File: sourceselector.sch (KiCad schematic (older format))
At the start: 31 parts, among them J14 RCAJack, J15 RCAJack, J16 RCAJack, J17 RCAJack, J18 RCAJack, J19 RCAJack, J20 RCAJack, J21 RCAJack, J22 Jack-DC, J23 Conn_01x02, J24 Conn_01x02, SW2 SW_SPST, SW3 SW_SPST

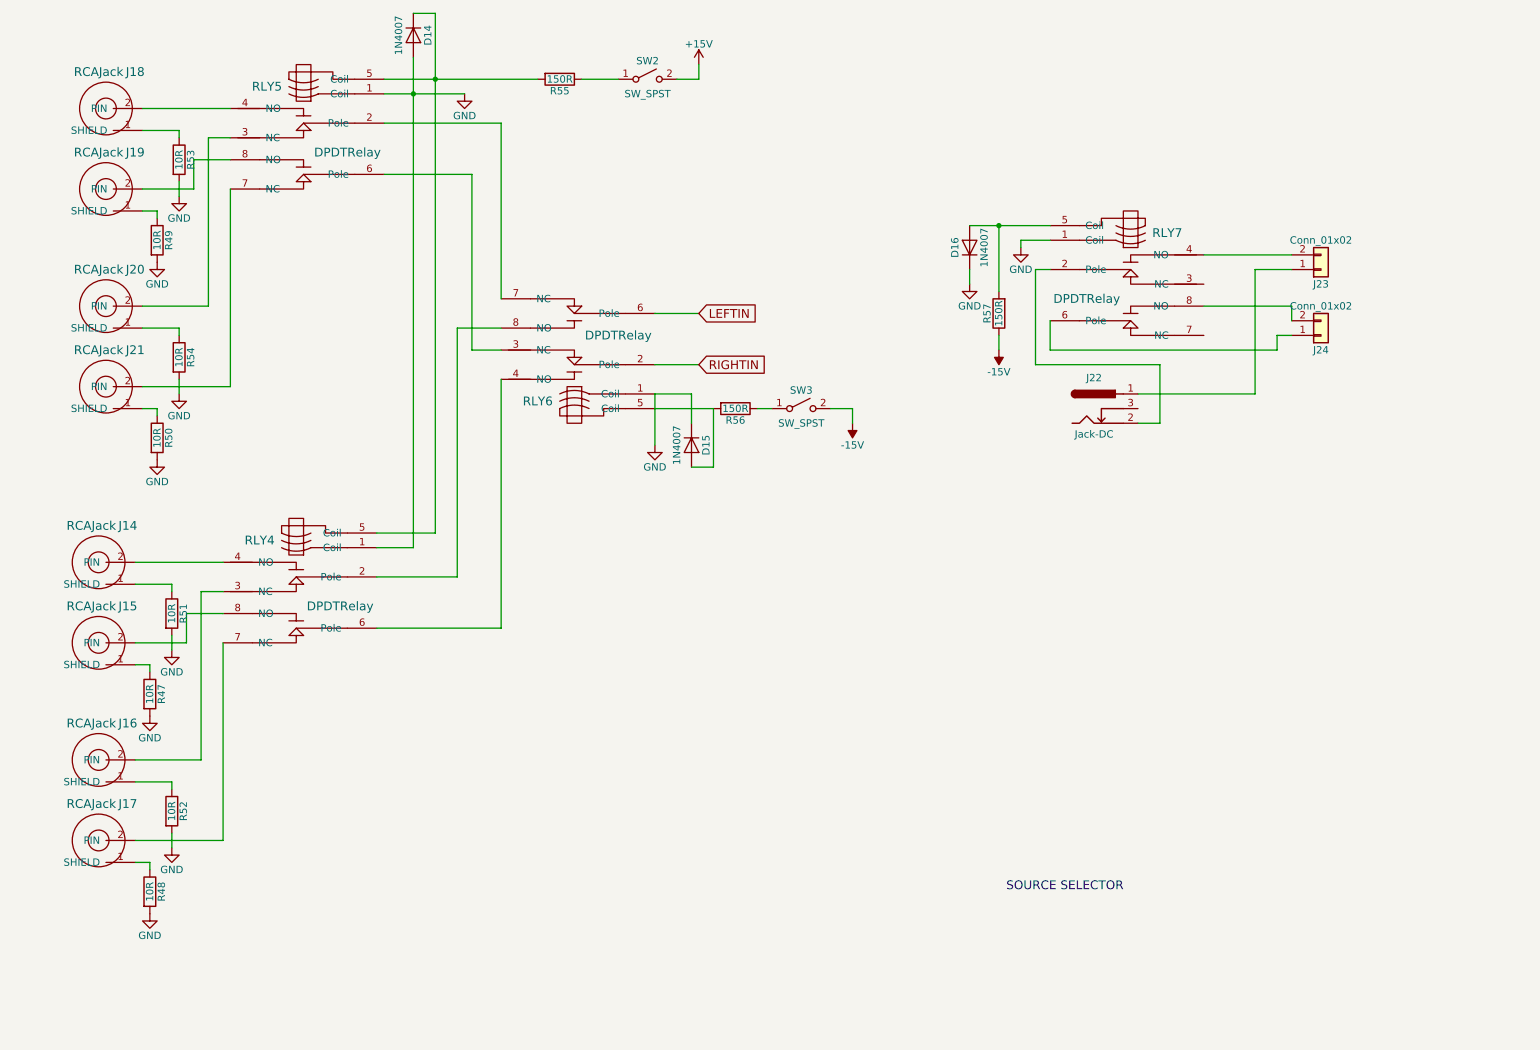
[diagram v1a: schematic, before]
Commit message: Changed one input to be balanced
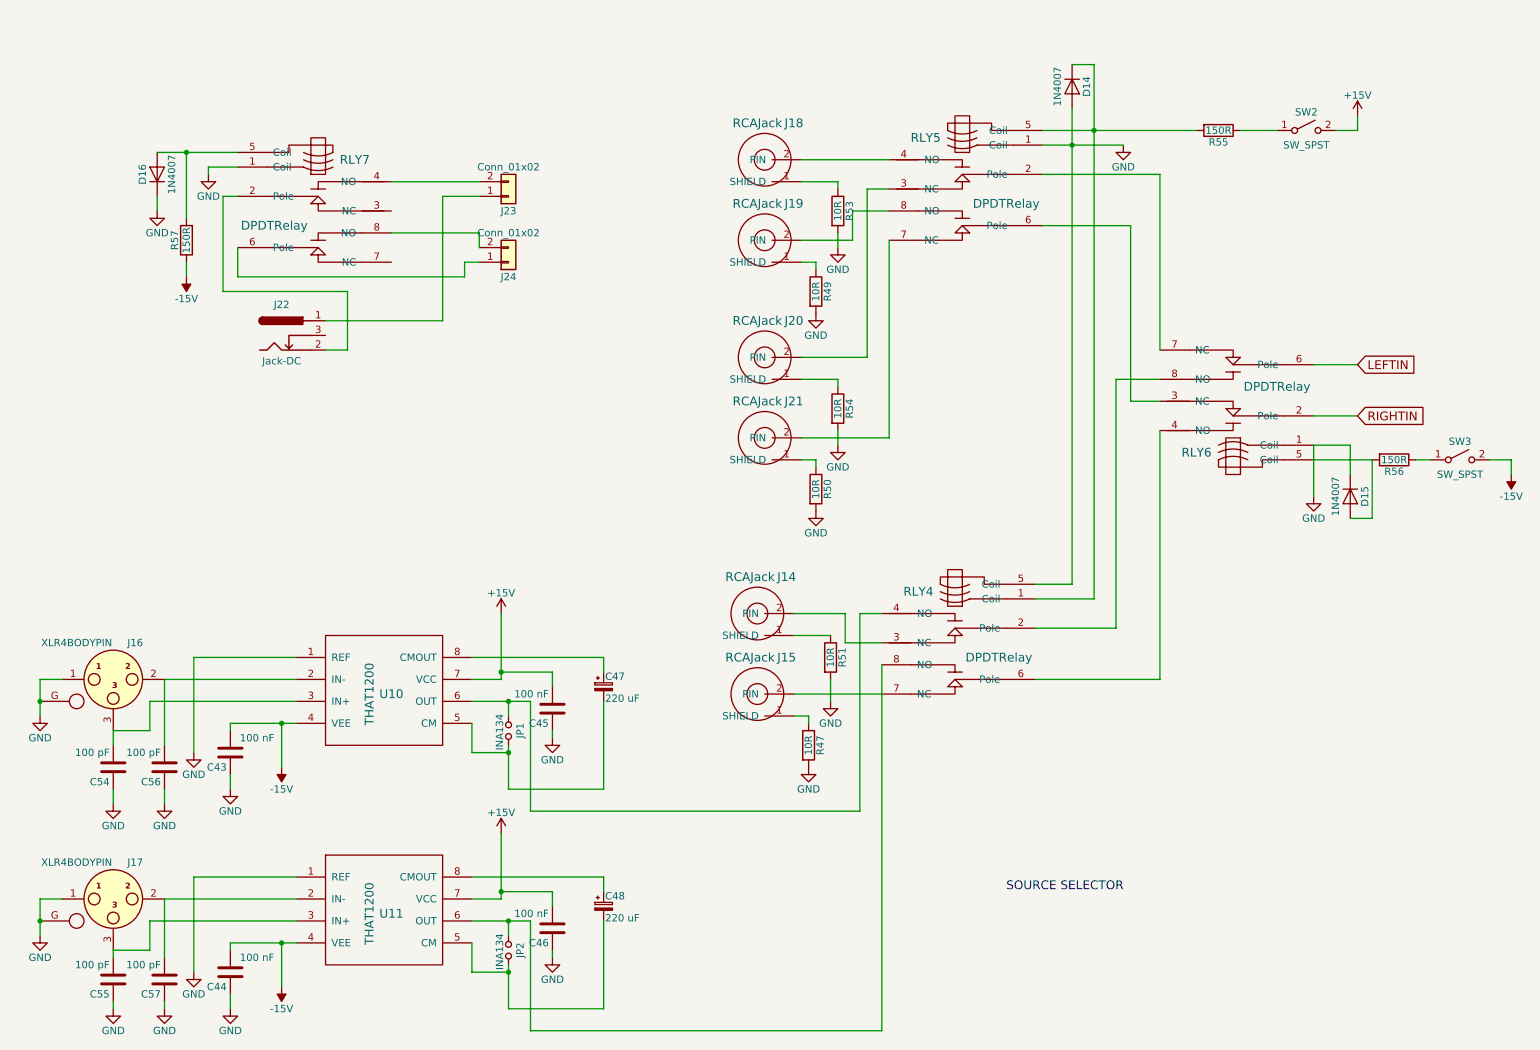
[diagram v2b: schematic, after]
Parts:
- removed J16, J17: RCAJack, Preamp:RCAConnectorCommon, symbol RCAJack
- removed R48, R52: 10R, Resistors_THT:R_Axial_DIN0207_L6.3mm_D2.5mm_P7.62mm_Horizontal, symbol R
- added C43, C44, C45, C46: 100 nF, Capacitors_THT:C_Disc_D5.0mm_W2.5mm_P5.00mm, symbol C
- added C47, C48: 220 uF, Capacitors_THT:CP_Radial_D7.5mm_P2.50mm, symbol CP_Small
- added C54, C55, C56, C57: 100 pF, Capacitors_THT:C_Disc_D5.0mm_W2.5mm_P5.00mm, symbol C
- added J16, J17: XLR4BODYPIN, Preamp:IOXLR3FEH, symbol XLR4BODYPIN
- added JP1, JP2: INA134, Pin_Headers:Pin_Header_Straight_1x02_Pitch2.54mm, symbol Jumper_NO_Small
- added U10, U11: THAT1200, Housings_DIP:DIP-8_W7.62mm_Socket, symbol THAT1200
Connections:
- net +15V: now also C45.2, C46.2, U10.7 (VCC), U11.7 (VCC)
- net -15V: now also C43.2, C44.2, U10.4 (VEE), U11.4 (VEE)
- net GND: now also RLY4.5 (Coil), C43.1, C44.1, C45.1, C46.1, C54.1, C55.1, C56.1, C57.1, J16.1, J16.G, J17.1, J17.G, U10.1 (REF), U11.1 (REF); no longer RLY4.1 (Coil)
- net at D14.1 (K), R55.2, RLY5.5 (Coil): now also RLY4.1 (Coil); no longer RLY4.5 (Coil)
- net at RLY4.3 (NC): now also J14.2 (PIN)
- net at RLY4.4 (NO): now also JP1.1, U10.6 (OUT); no longer J14.2 (PIN)
- net at RLY4.7 (NC): now also J15.2 (PIN)
- net at RLY4.8 (NO): now also JP2.1, U11.6 (OUT); no longer J15.2 (PIN)
- new net: C56.2, J16.2, U10.2 (IN-)
- new net: C54.2, J16.3, U10.3 (IN+)
- new net: C47.2, JP1.2, U10.5 (CM)
- new net: C47.1, U10.8 (CMOUT)
- new net: C57.2, J17.2, U11.2 (IN-)
- new net: C55.2, J17.3, U11.3 (IN+)
- new net: C48.2, JP2.2, U11.5 (CM)
- new net: C48.1, U11.8 (CMOUT)
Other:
- moved on the sheet: D14, D15, D16, J14, J15, J18, J19, J20, J21, J22, J23, J24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

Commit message: JLCPCB 2021-03-26
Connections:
- net GND: now also C54.2, C55.2; no longer C54.1, C55.1
- net at C56.2, J16.2: now also U10.3 (IN+); no longer U10.2 (IN-)
- net at C57.2, J17.2: now also U11.3 (IN+); no longer U11.2 (IN-)
- new net: C54.1, J16.3, U10.2 (IN-)
- new net: C55.1, J17.3, U11.2 (IN-)
- no-connect marks 0 -> 2
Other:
- moved on the sheet: C54, C55, J17

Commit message: Pre off relay
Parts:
- removed R55, R56, R57: 150R, Resistors_THT:R_Axial_DIN0309_L9.0mm_D3.2mm_P12.70mm_Horizontal, symbol R
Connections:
- net -15V: now also D16.2 (A), RLY7.5 (Coil)
- net at D14.1 (K), RLY4.1 (Coil), RLY5.5 (Coil): now also SW2.1 (A)
- net at D15.2 (A), RLY6.5 (Coil): now also SW3.1 (A)
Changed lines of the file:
@@
 RIGHTIN
-$Comp
-L R R55
-U 1 1 60563808
-P 8850 1600
-F 0 "R55" V 8930 1600 50  0000 C CNN
-F 1 "150R" V 8850 1600 50  0000 C CNN
-F 2 "Resistors_THT:R_Axial_DIN0309_L9.0mm_D3.2mm_P12.70mm_Horizontal" V 8780 1600 50  0001 C CNN
-F 3 "" H 8850 1600 50  0001 C CNN
-	1    8850 1600
-	0    1    1    0
-$EndComp
 $Comp
 L SW_SPST SW2
@@
 $EndComp
 $Comp
-L R R56
-U 1 1 60564003
-P 10050 3850
-F 0 "R56" V 10130 3850 50  0000 C CNN
-F 1 "150R" V 10050 3850 50  0000 C CNN
-F 2 "Resistors_THT:R_Axial_DIN0309_L9.0mm_D3.2mm_P12.70mm_Horizontal" V 9980 3850 50  0001 C CNN
-F 3 "" H 10050 3850 50  0001 C CNN
-	1    10050 3850
-	0    1    1    0
-$EndComp
-$Comp
 L SW_SPST SW3
 U 1 1 60564101
@@
 $EndComp
 $Comp
-L -15V #PWR90
+L -15V #PWR88
 U 1 1 6056426E
 P 10850 3950
-F 0 "#PWR90" H 10850 4050 50  0001 C CNN
+F 0 "#PWR88" H 10850 4050 50  0001 C CNN
 F 1 "-15V" H 10850 4100 50  0000 C CNN
 F 2 "" H 10850 3950 50  0001 C CNN
@@
 $EndComp
 $Comp
-L -15V #PWR69
+L -15V #PWR67
 U 1 1 604F8C40
 P 1800 2600
-F 0 "#PWR69" H 1800 2700 50  0001 C CNN
+F 0 "#PWR67" H 1800 2700 50  0001 C CNN
 F 1 "-15V" H 1800 2750 50  0000 C CNN
 F 2 "" H 1800 2600 50  0001 C CNN
@@
 $EndComp
 $Comp
-L R R57
-U 1 1 604F8F82
-P 1800 2350
-F 0 "R57" V 1880 2350 50  0000 C CNN
-F 1 "150R" V 1800 2350 50  0000 C CNN
-F 2 "Resistors_THT:R_Axial_DIN0309_L9.0mm_D3.2mm_P12.70mm_Horizontal" V 1730 2350 50  0001 C CNN
-F 3 "" H 1800 2350 50  0001 C CNN
-	1    1800 2350
-	-1   0    0    1
-$EndComp
-$Comp
 L D D16
 U 1 1 604F927C
@@
 $EndComp
 $Comp
-L -15V #PWR75
+L -15V #PWR73
 U 1 1 60533183
 P 2450 5950
-F 0 "#PWR75" H 2450 6050 50  0001 C CNN
+F 0 "#PWR73" H 2450 6050 50  0001 C CNN
 F 1 "-15V" H 2450 6100 50  0000 C CNN
 F 2 "" H 2450 5950 50  0001 C CNN
@@
 $EndComp
 $Comp
-L -15V #PWR76
+L -15V #PWR74
 U 1 1 60535F3C
 P 2450 7450
-F 0 "#PWR76" H 2450 7550 50  0001 C CNN
+F 0 "#PWR74" H 2450 7550 50  0001 C CNN
 F 1 "-15V" H 2450 7600 50  0000 C CNN
 F 2 "" H 2450 7450 50  0001 C CNN
@@
 	9500 3750 9500 4100
 Wire Wire Line
-	9900 3850 9500 3850
+	9500 3850 10300 3850
 Wire Wire Line
 	3700 2500 3800 2500
@@
 	1600 1750 2150 1750
 Wire Wire Line
-	1800 2600 1800 2500
-Wire Wire Line
-	1800 1750 1800 2200
+	1800 1750 1800 2600
 Wire Wire Line
 	7850 1150 8000 1150
@@
 Wire Wire Line
 	10850 3850 10850 3950
-Wire Wire Line
-	10300 3850 10200 3850
 Connection ~ 7850 1700
 Wire Wire Line
@@
 	9800 1500 9800 1600
 Wire Wire Line
-	9250 1600 9000 1600
+	7650 1600 9250 1600
 Connection ~ 8000 1600
 Wire Wire Line
@@
 Wire Wire Line
 	8000 1150 8000 4800
-Wire Wire Line
-	7650 1600 8700 1600
 Wire Wire Line
 	7650 1700 8200 1700
@@
 Wire Wire Line
 	8450 5350 8450 3650
+Connection ~ 9900 3850
 $EndSCHEMATC

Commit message: Tried a relay version out
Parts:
- added R23, R43: 22R, Resistors_THT:R_Axial_DIN0309_L9.0mm_D3.2mm_P12.70mm_Horizontal, symbol R
- added RLY8: DPDTRelay, Preamp:G2VRelay, symbol DPDTRelay
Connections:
- net +15V: now also RLY8.5 (Coil), RLY8.6 (Pole)
- net -15V: now also RLY8.2 (Pole)
- net GND: now also R23.2, R43.2, RLY8.1 (Coil)
- new net: R23.1, RLY8.3 (NC)
- new net: R43.1, RLY8.7 (NC)
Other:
- moved on the sheet: D16, J22, J23, J24, RLY7

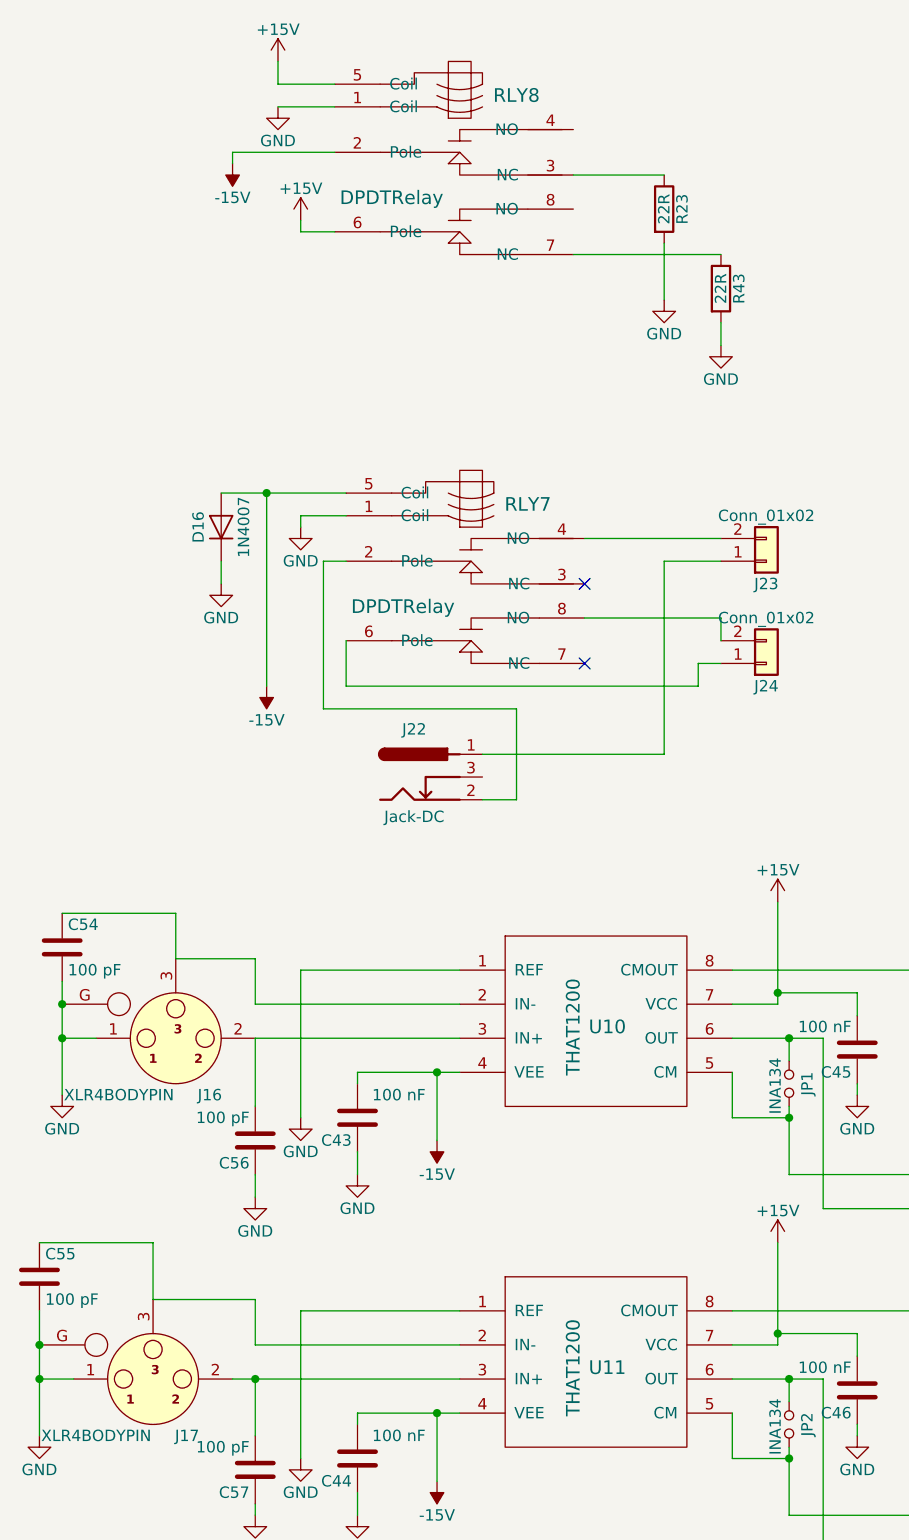
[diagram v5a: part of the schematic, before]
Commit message: Put larger capacitors on
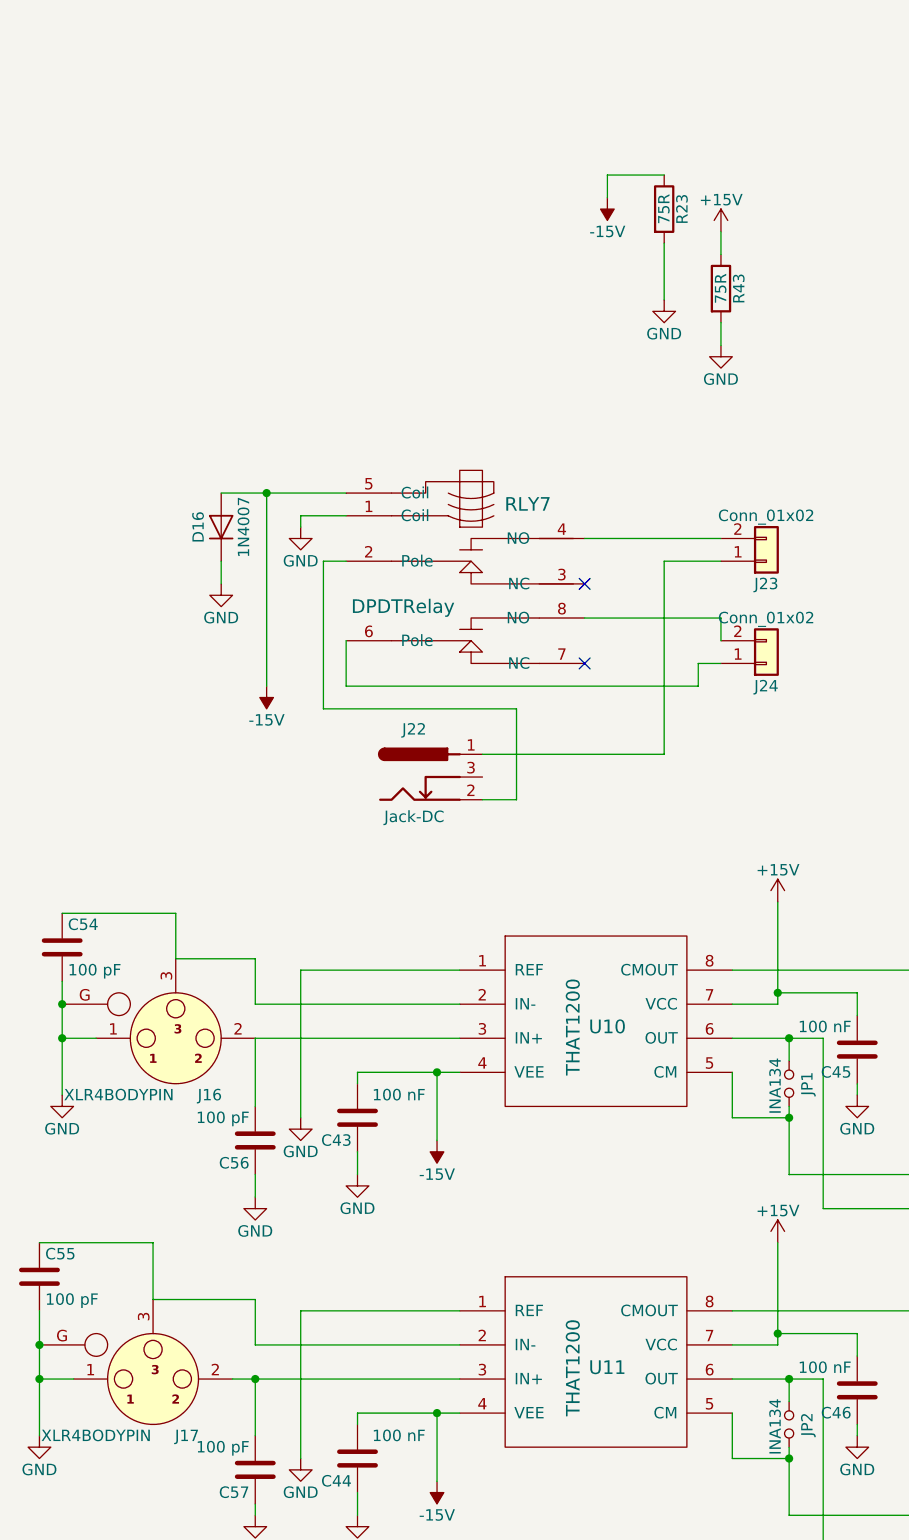
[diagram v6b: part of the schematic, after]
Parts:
- removed RLY8: DPDTRelay, Preamp:G2VRelay, symbol DPDTRelay
- R23, R43: value 22R -> 75R
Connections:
- net +15V: now also R43.1
- net -15V: now also R23.1
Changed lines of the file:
@@
 NoConn ~ 3100 3850
-$Comp
-L DPDTRelay RLY8
-U 1 1 60697858
-P 2550 1500
-F 0 "RLY8" H 2800 1350 60  0000 C CNN
-F 1 "DPDTRelay" H 2250 1800 60  0000 C CNN
-F 2 "Preamp:G2VRelay" H 2550 1500 60  0001 C CNN
-F 3 "" H 2550 1500 60  0001 C CNN
-	1    2550 1500
-	1    0    0    1
-$EndComp
 $Comp
 L R R43
@@
 P 3700 2200
 F 0 "R43" V 3780 2200 50  0000 C CNN
-F 1 "22R" V 3700 2200 50  0000 C CNN
+F 1 "75R" V 3700 2200 50  0000 C CNN
 F 2 "Resistors_THT:R_Axial_DIN0309_L9.0mm_D3.2mm_P12.70mm_Horizontal" V 3630 2200 50  0001 C CNN
 F 3 "" H 3700 2200 50  0001 C CNN
@@
 P 3450 1850
 F 0 "R23" V 3530 1850 50  0000 C CNN
-F 1 "22R" V 3450 1850 50  0000 C CNN
+F 1 "75R" V 3450 1850 50  0000 C CNN
 F 2 "Resistors_THT:R_Axial_DIN0309_L9.0mm_D3.2mm_P12.70mm_Horizontal" V 3380 1850 50  0001 C CNN
 F 3 "" H 3450 1850 50  0001 C CNN
@@
 L -15V #PWR71
 U 1 1 60698793
-P 1550 1650
-F 0 "#PWR71" H 1550 1750 50  0001 C CNN
-F 1 "-15V" H 1550 1800 50  0000 C CNN
-F 2 "" H 1550 1650 50  0001 C CNN
-F 3 "" H 1550 1650 50  0001 C CNN
-	1    1550 1650
+P 3200 1800
+F 0 "#PWR71" H 3200 1900 50  0001 C CNN
+F 1 "-15V" H 3200 1950 50  0000 C CNN
+F 2 "" H 3200 1800 50  0001 C CNN
+F 3 "" H 3200 1800 50  0001 C CNN
+	1    3200 1800
 	-1   0    0    1
 $EndComp
 $Comp
 L +15V #PWR079
-U 1 1 606989C7
-P 1850 1900
-F 0 "#PWR079" H 1850 1750 50  0001 C CNN
-F 1 "+15V" H 1850 2040 50  0000 C CNN
-F 2 "" H 1850 1900 50  0001 C CNN
-F 3 "" H 1850 1900 50  0001 C CNN
-	1    1850 1900
-	1    0    0    -1
-$EndComp
-$Comp
-L +15V #PWR080
 U 1 1 60698C28
-P 1750 1200
-F 0 "#PWR080" H 1750 1050 50  0001 C CNN
-F 1 "+15V" H 1750 1340 50  0000 C CNN
-F 2 "" H 1750 1200 50  0001 C CNN
-F 3 "" H 1750 1200 50  0001 C CNN
-	1    1750 1200
-	1    0    0    -1
-$EndComp
-$Comp
-L GND #PWR081
-U 1 1 60698DB3
-P 1750 1400
-F 0 "#PWR081" H 1750 1150 50  0001 C CNN
-F 1 "GND" H 1750 1250 50  0000 C CNN
-F 2 "" H 1750 1400 50  0001 C CNN
-F 3 "" H 1750 1400 50  0001 C CNN
-	1    1750 1400
-	1    0    0    -1
-$EndComp
-Wire Wire Line
-	1550 1600 1550 1650
-Wire Wire Line
-	3700 2050 3050 2050
-Wire Wire Line
-	2000 1400 1750 1400
-Wire Wire Line
-	1750 1300 1750 1200
-Wire Wire Line
-	2000 1300 1750 1300
-Wire Wire Line
-	2000 1600 1550 1600
-Wire Wire Line
-	1850 1950 2000 1950
-Wire Wire Line
-	1850 1900 1850 1950
+P 3700 1950
+F 0 "#PWR079" H 3700 1800 50  0001 C CNN
+F 1 "+15V" H 3700 2090 50  0000 C CNN
+F 2 "" H 3700 1950 50  0001 C CNN
+F 3 "" H 3700 1950 50  0001 C CNN
+	1    3700 1950
+	1    0    0    -1
+$EndComp
 Wire Wire Line
 	3700 2450 3700 2350
 Wire Wire Line
 	3450 2250 3450 2000
-Wire Wire Line
-	3050 1700 3450 1700
 Connection ~ 9900 3850
 Wire Wire Line
@@
 	1650 5500 2550 5500
 Wire Wire Line
-	1300 4950 1300 5150
-Wire Wire Line
-	800  4950 1300 4950
+	1300 5150 1300 4950
+Wire Wire Line
+	1300 4950 800  4950
 Connection ~ 800  5350
 Connection ~ 800  5500
@@
 Connection ~ 700  7000
 Wire Wire Line
-	850  7000 700  7000
+	700  7000 850  7000
 Connection ~ 700  6850
 Wire Wire Line
@@
 Wire Wire Line
 	6550 7750 6550 5250
+Wire Wire Line
+	3700 1950 3700 2050
+Wire Wire Line
+	3200 1800 3200 1700
+Wire Wire Line
+	3200 1700 3450 1700
 $EndSCHEMATC
